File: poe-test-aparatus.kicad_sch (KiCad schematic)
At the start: 31 parts, among them J1 Power Injector, J2 PoE Header, U3 MP8007, U4 POE70P-12L

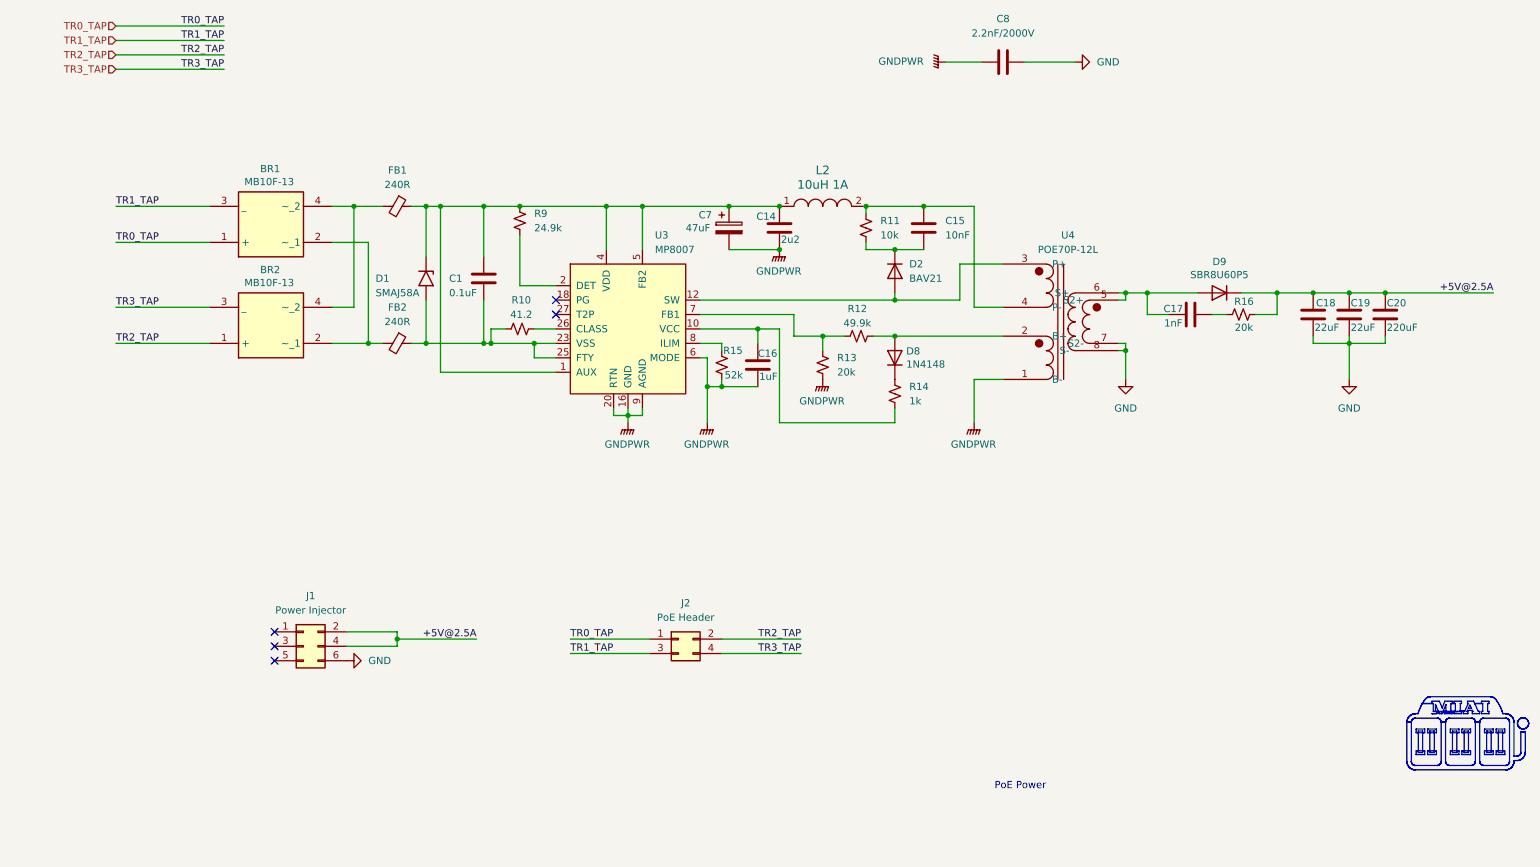
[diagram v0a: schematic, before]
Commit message: Rework with better layout and resistors fix tests
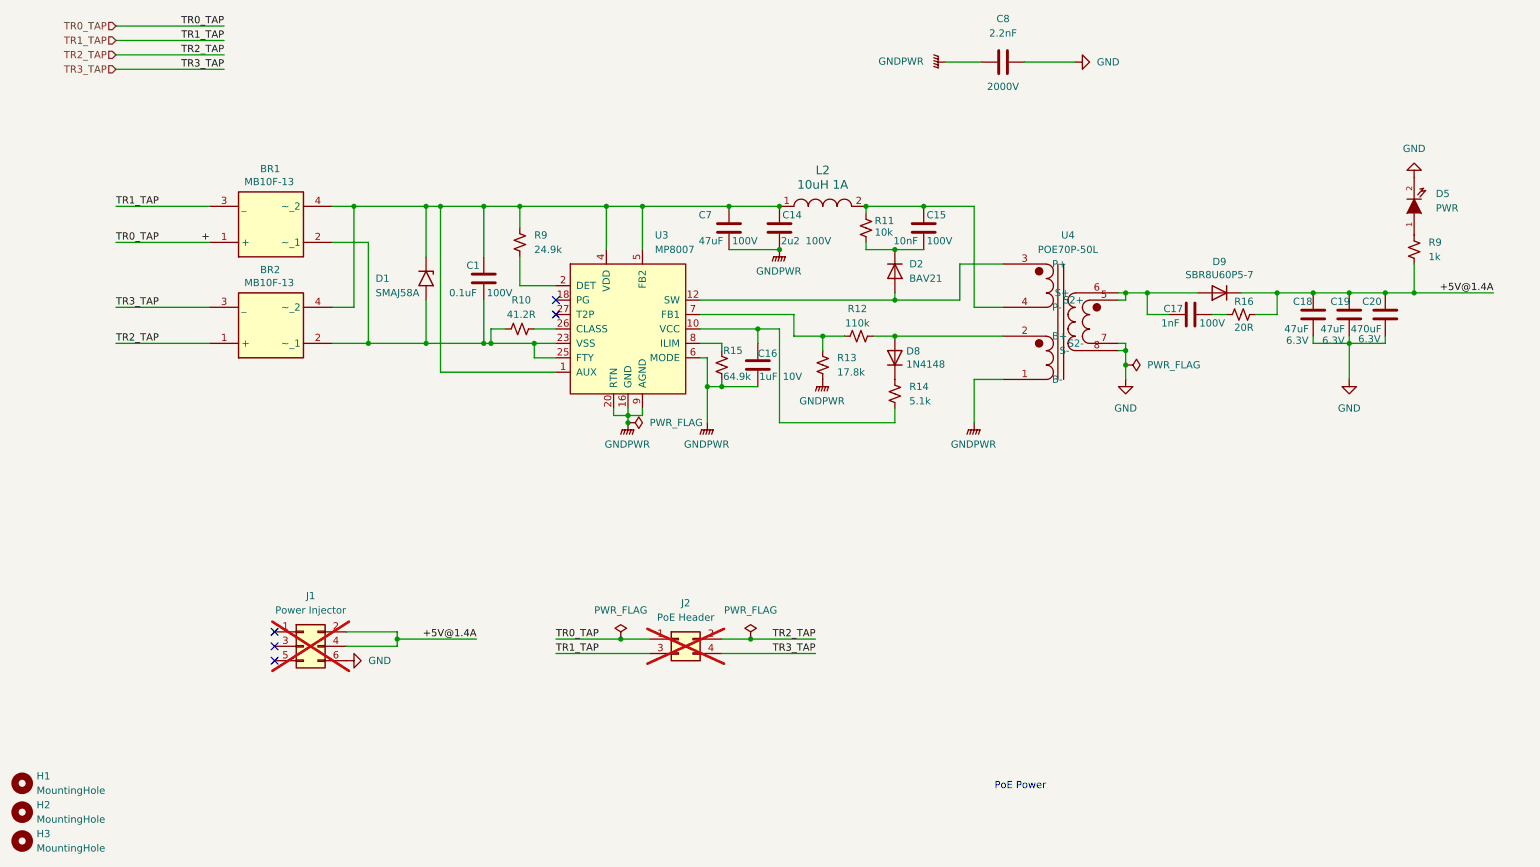
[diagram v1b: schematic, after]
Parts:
- removed FB1, FB2: 240R, PowerManagement:BLM31KN102BH1L, symbol Device:FerriteBead_Small
- added D5: PWR, LED_SMD:LED_1206_3216Metric, symbol tinkerforge:LED
- added H1, H2, H3: MountingHole, MountingHole:MountingHole_3.2mm_M3_ISO14580, symbol Mechanical:MountingHole
- added R9: 1k, Resistor_SMD:R_1206_3216Metric_Pad1.30x1.75mm_HandSolder, symbol Device:R_Small_US
- C1, C14, C15, C17: Voltage (none) -> 100V
- C16: Voltage (none) -> 10V
- C18, C19: value 22uF -> 47uF; Voltage (none) -> 6.3V
- C20: value 220uF -> 470uF; footprint Capacitor_SMD:C_1206_3216Metric_Pad1.33x1.80mm_HandSolder -> Capacitor_Tantalum_SMD:CP_EIA-7343-43_Kemet-X; Voltage (none) -> 6.3V
- C7: footprint Capacitor_SMD:CP_Elec_5x5.4 -> Capacitor_SMD:C_1210_3225Metric; symbol Device:C_Polarized -> Device:C; Voltage (none) -> 100V
- C8: value 2.2nF/2000V -> 2.2nF; footprint Capacitor_SMD:C_1206_3216Metric_Pad1.33x1.80mm_HandSolder -> Capacitor_SMD:C_1825_4564Metric; Voltage (none) -> 2000V
- D9: value SBR8U60P5 -> SBR8U60P5-7
- J1, J2: now not fitted
- L2: footprint Inductor_SMD:L_Bourns_SRU5016_5.2x5.2mm -> InductorAlt:INDPM3532X120N
- R10: value 41.2 -> 41.2R
- R12: value 49.9k -> 110k
- R13: value 20k -> 17.8k
- R14: value 1k -> 5.1k
- R15: value 52k -> 64.9k
- R16: value 20k -> 20R
- U4: value POE70P-12L -> POE70P-50L; footprint PoweredDevices:POE70P12LD -> PoweredDevices:POE70P50LD
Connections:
- net GND: now also D5.2 (K)
- net at C1.1, C14.1, C7.1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: now also BR1.4 (~_2), BR2.4 (~_2)
- net at C1.2, D1.2 (A2), R10.1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: now also BR1.2 (~_1), BR2.2 (~_1)
- net +5V@2.5A renamed +5V@1.4A
- net +5V@1.4A: now also R9.2
- new net: D5.1 (A), R9.1
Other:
- moved on the sheet: R9

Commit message: moderate updates
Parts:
- removed L2: 10uH 1A, InductorAlt:INDPM3532X120N, symbol tinkerforge:INDUCTOR
- added J3: Conn_01x02_Pin, Connector_JST:JST_SH_SM02B-SRSS-TB_1x02-1MP_P1.00mm_Horizontal, symbol Connector:Conn_01x02_Pin
- C7: value 47uF -> 10uF
- R14: value 5.1k -> 1k
- R15: value 64.9k -> 49.9k
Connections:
- net +5V@1.4A: now also J3.1 (Pin_1); no longer R9.2
- net GND: now also J3.2 (Pin_2); no longer D5.2 (K)
- net at BR1.4 (~_2), BR2.4 (~_2), C1.1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: now also C15.1, R11.1, R9.1, U4.4 (P-)
- net at U3.27 (T2P): now also D5.2 (K)
- net at D5.1 (A): now also R9.2; no longer R9.1
- net TR0_TAP renamed +
- no-connect marks 5 -> 4
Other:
- moved on the sheet: C1, R9

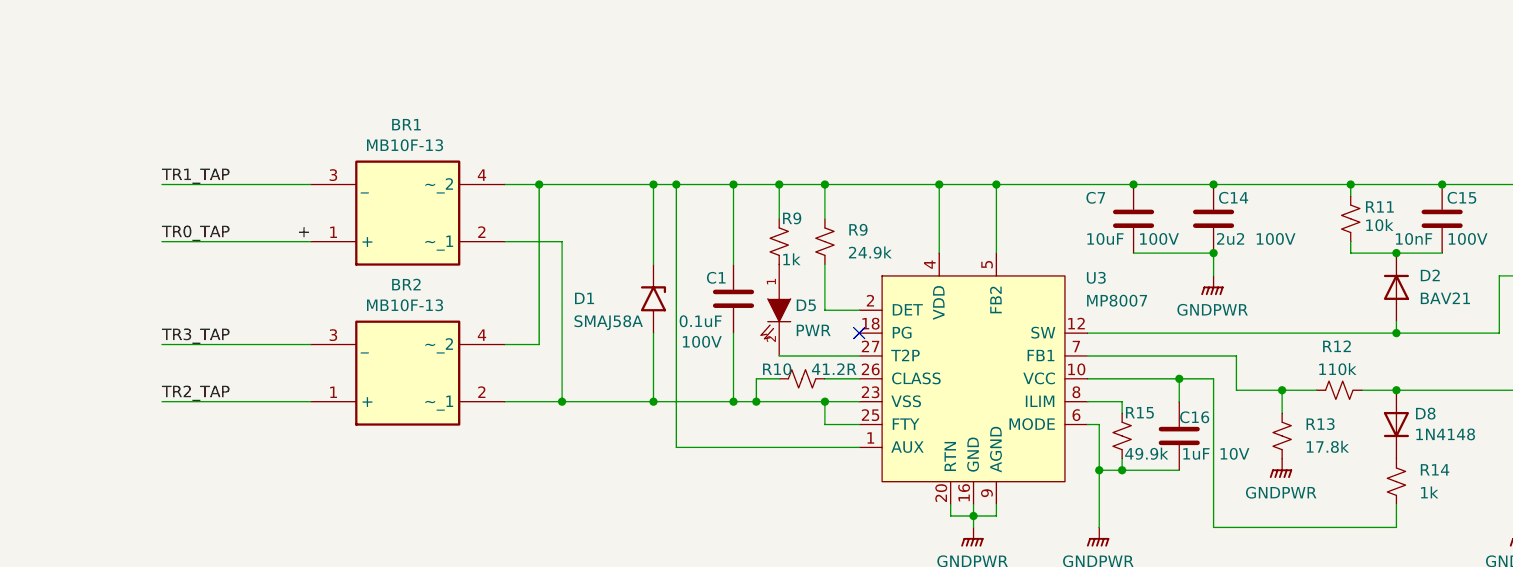
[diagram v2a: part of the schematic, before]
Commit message: Fixed flipped rectifier diode input
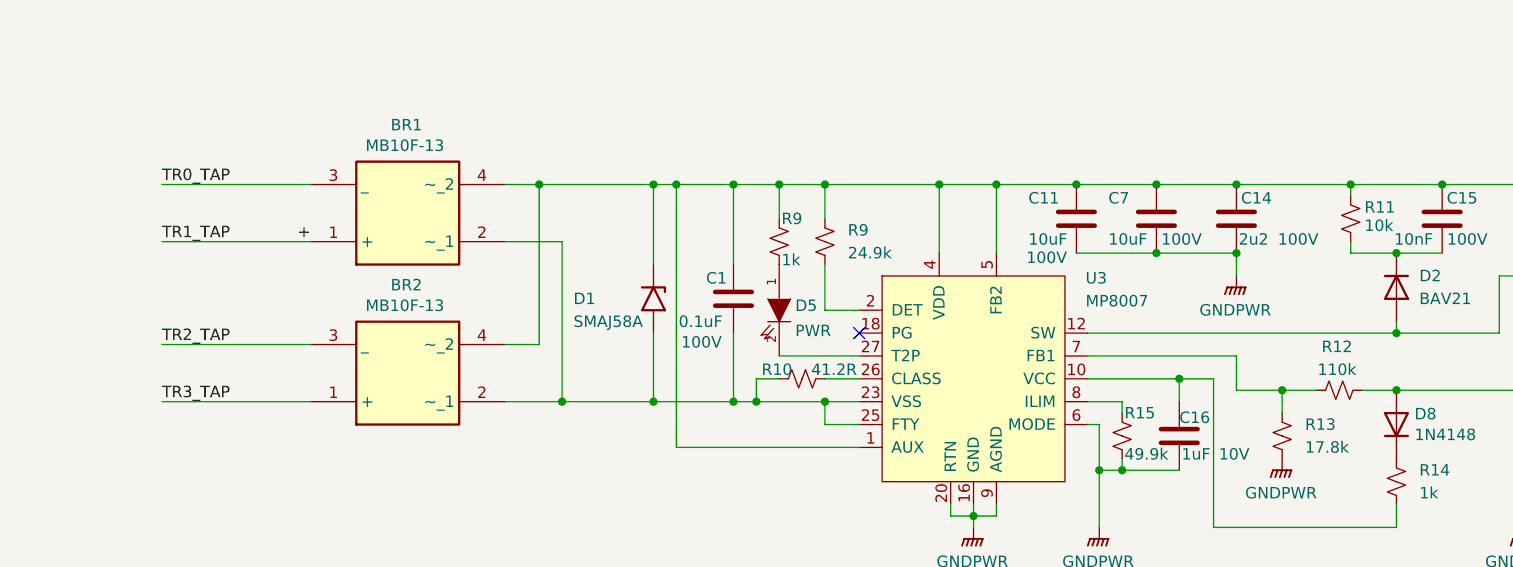
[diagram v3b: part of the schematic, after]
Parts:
- added C11: 10uF, Capacitor_SMD:C_1210_3225Metric, symbol Device:C
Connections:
- net +: now also J2.3 (Pin_3); no longer J2.1 (Pin_1)
- net GNDPWR: now also C11.2
- net TR2_TAP: now also BR2.3 (_); no longer BR2.1 (+)
- net TR3_TAP: now also BR2.1 (+); no longer BR2.3 (_)
- net at BR1.4 (~_2), BR2.4 (~_2), C1.1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: now also C11.1
- net TR1_TAP renamed TR0_TAP
- net TR0_TAP: now also J2.1 (Pin_1); no longer J2.3 (Pin_3)
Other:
- moved on the sheet: C14, C7
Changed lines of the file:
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@@
 	)
 	(junction
-		(at 212.09 106.68)
+		(at 144.78 81.28)
 		(diameter 0)
 		(color 0 0 0 0)
 	)
 	(junction
-		(at 212.09 96.52)
+		(at 212.09 106.68)
 		(diameter 0)
 		(color 0 0 0 0)
 	)
 	(junction
-		(at 158.75 104.14)
+		(at 212.09 96.52)
 		(diameter 0)
 		(color 0 0 0 0)
 	)
 	(junction
-		(at 171.45 97.79)
+		(at 158.75 104.14)
 		(diameter 0)
 		(color 0 0 0 0)
 	)
 	(junction
-		(at 151.13 81.28)
+		(at 171.45 97.79)
 		(diameter 0)
 		(color 0 0 0 0)
@@
 	)
 	(junction
+		(at 153.67 81.28)
+		(diameter 0)
+		(color 0 0 0 0)
+	)
+	(junction
+		(at 135.89 81.28)
+		(diameter 0)
+		(color 0 0 0 0)
+	)
+	(junction
 		(at 107.95 105.41)
 		(diameter 0)
@@
 	)
 	(junction
-		(at 151.13 88.9)
+		(at 153.67 88.9)
 		(diameter 0)
 		(color 0 0 0 0)
@@
 	)
 	(junction
-		(at 142.24 81.28)
+		(at 144.78 88.9)
 		(diameter 0)
 		(color 0 0 0 0)
@@
 	(wire
 		(pts
-			(xy 151.13 81.28) (xy 166.37 81.28)
-		)
-		(stroke
-			(width 0)
-			(type default)
-		)
-	)
-	(wire
-		(pts
 			(xy 100.33 105.41) (xy 107.95 105.41)
 		)
@@
 	(wire
 		(pts
+			(xy 144.78 81.28) (xy 153.67 81.28)
+		)
+		(stroke
+			(width 0)
+			(type default)
+		)
+	)
+	(wire
+		(pts
 			(xy 72.39 81.28) (xy 76.2 81.28)
 		)
@@
 	(wire
 		(pts
-			(xy 142.24 81.28) (xy 151.13 81.28)
-		)
-		(stroke
-			(width 0)
-			(type default)
-		)
-	)
-	(wire
-		(pts
 			(xy 107.95 95.25) (xy 111.76 95.25)
 		)
@@
 	(wire
 		(pts
-			(xy 151.13 88.9) (xy 151.13 91.44)
+			(xy 153.67 88.9) (xy 153.67 91.44)
 		)
 		(stroke
@@
 	(wire
 		(pts
+			(xy 135.89 88.9) (xy 144.78 88.9)
+		)
+		(stroke
+			(width 0)
+			(type default)
+		)
+	)
+	(wire
+		(pts
 			(xy 107.95 102.87) (xy 111.76 102.87)
 		)
@@
 	(wire
 		(pts
+			(xy 153.67 81.28) (xy 166.37 81.28)
+		)
+		(stroke
+			(width 0)
+			(type default)
+		)
+	)
+	(wire
+		(pts
 			(xy 34.29 99.06) (xy 50.8 99.06)
 		)
@@
 	(wire
 		(pts
-			(xy 142.24 88.9) (xy 151.13 88.9)
+			(xy 135.89 81.28) (xy 144.78 81.28)
+		)
+		(stroke
+			(width 0)
+			(type default)
+		)
+	)
+	(wire
+		(pts
+			(xy 144.78 88.9) (xy 153.67 88.9)
 		)
 		(stroke
@@
 	(wire
 		(pts
-			(xy 127 81.28) (xy 142.24 81.28)
+			(xy 127 81.28) (xy 135.89 81.28)
 		)
 		(stroke
@@
 		)
 	)
-	(label "TR1_TAP"
-		(at 116.84 160.02 0)
+	(label "TR3_TAP"
+		(at 34.29 105.41 0)
 		(fields_autoplaced yes)
 		(effects
@@
 	)
 	(label "TR1_TAP"
-		(at 34.29 81.28 0)
+		(at 116.84 160.02 0)
 		(fields_autoplaced yes)
 		(effects
@@
 		)
 	)
-	(label "+5V@1.4A"
-		(at 95.25 157.48 180)
+	(label "TR0_TAP"
+		(at 34.29 81.28 0)
 		(fields_autoplaced yes)
 		(effects
@@
 				(size 1.27 1.27)
 			)
-			(justify right bottom)
+			(justify left bottom)
 		)
 	)
-	(label "TR3_TAP"
-		(at 152.4 160.02 180)
+	(label "+5V@1.4A"
+		(at 95.25 157.48 180)
 		(fields_autoplaced yes)
 		(effects
@@
 		)
 	)
-	(label "TR0_TAP"
-		(at 116.84 157.48 0)
+	(label "TR1_TAP"
+		(at 34.29 87.63 0)
 		(fields_autoplaced yes)
 		(effects
@@
 		)
 	)
-	(label "+5V@1.4A"
-		(at 276.86 96.52 180)
+	(label "TR2_TAP"
+		(at 34.29 99.06 0)
 		(fields_autoplaced yes)
 		(effects
@@
 				(size 1.27 1.27)
 			)
-			(justify right bottom)
+			(justify left bottom)
 		)
 	)
-	(label "TR2_TAP"
-		(at 34.29 105.41 0)
+	(label "TR3_TAP"
+		(at 152.4 160.02 180)
 		(fields_autoplaced yes)
 		(effects
@@
 				(size 1.27 1.27)
 			)
-			(justify left bottom)
+			(justify right bottom)
 		)
 	)
-	(label "TR3_TAP"
-		(at 34.29 99.06 0)
+	(label "TR0_TAP"
+		(at 116.84 157.48 0)
 		(fields_autoplaced yes)
 		(effects
@@
 		)
 	)
-	(label "TR0_TAP"
-		(at 34.29 87.63 0)
+	(label "+5V@1.4A"
+		(at 276.86 96.52 180)
 		(fields_autoplaced yes)
 		(effects
@@
 				(size 1.27 1.27)
 			)
-			(justify left bottom)
+			(justify right bottom)
 		)
 	)
@@
 	(symbol
 		(lib_id "Device:C")
-		(at 142.24 85.09 0)
+		(at 144.78 85.09 0)
 		(unit 1)
 		(exclude_from_sim no)
@@
 		(dnp no)
 		(property "Reference" "C7"
-			(at 136.906 82.804 0)
+			(at 139.446 82.804 0)
 			(effects
 				(font
@@
 		)
 		(property "Value" "10uF"
-			(at 136.906 87.376 0)
+			(at 139.446 87.376 0)
 			(effects
 				(font
@@
 		)
 		(property "Footprint" "Capacitor_SMD:C_1210_3225Metric"
-			(at 143.2052 88.9 0)
+			(at 145.7452 88.9 0)
 			(effects
 				(font
@@
 		)
 		(property "Datasheet" "~"
-			(at 142.24 85.09 0)
+			(at 144.78 85.09 0)
 			(effects
 				(font
@@
 		)
 		(property "Description" "Unpolarized capacitor"
-			(at 142.24 85.09 0)
+			(at 144.78 85.09 0)
 			(effects
 				(font
@@
 		)
 		(property "Voltage" "100V"
-			(at 145.034 87.376 0)
+			(at 147.574 87.376 0)
 			(effects
 				(font
@@
 	(symbol
 		(lib_id "Device:C")
-		(at 151.13 85.09 0)
+		(at 153.67 85.09 0)
 		(unit 1)
 		(exclude_from_sim no)
@@
 		(dnp no)
 		(property "Reference" "C14"
-			(at 151.638 82.804 0)
+			(at 154.178 82.804 0)
 			(effects
 				(font
@@
 		)
 		(property "Value" "2u2"
-			(at 151.384 87.376 0)
+			(at 153.924 87.376 0)
 			(effects
 				(font
@@
 		)
 		(property "Footprint" "Capacitor_SMD:C_1206_3216Metric_Pad1.33x1.80mm_HandSolder"
-			(at 152.0952 88.9 0)
+			(at 154.6352 88.9 0)
 			(effects
 				(font
@@
 		)
 		(property "Datasheet" "~"
-			(at 151.13 85.09 0)
+			(at 153.67 85.09 0)
 			(effects
 				(font
@@
 		)
 		(property "Description" "Unpolarized capacitor"
-			(at 151.13 85.09 0)
+			(at 153.67 85.09 0)
 			(effects
 				(font
@@
 		)
 		(property "Voltage" "100V"
-			(at 157.988 87.376 0)
+			(at 160.528 87.376 0)
 			(effects
 				(font
@@
 	(symbol
 		(lib_id "power:GNDPWR")
-		(at 151.13 91.44 0)
+		(at 153.67 91.44 0)
 		(unit 1)
 		(exclude_from_sim no)
@@
 		(fields_autoplaced yes)
 		(property "Reference" "#PWR012"
-			(at 151.13 96.52 0)
+			(at 153.67 96.52 0)
 			(effects
 				(font
@@
 		)
 		(property "Value" "GNDPWR"
-			(at 151.003 95.25 0)
+			(at 153.543 95.25 0)
 			(effects
 				(font
@@
 		)
 		(property "Footprint" ""
-			(at 151.13 92.71 0)
+			(at 153.67 92.71 0)
 			(effects
 				(font
@@
 		)
 		(property "Datasheet" ""
-			(at 151.13 92.71 0)
+			(at 153.67 92.71 0)
 			(effects
 				(font
@@
 		)
 		(property "Description" "Power symbol creates a global label with name \"GNDPWR\" , global ground"
-			(at 151.13 91.44 0)
+			(at 153.67 91.44 0)
 			(effects
 				(font
@@
 					(unit 1)
 				)
+			)
+		)
+	)
+	(symbol
+		(lib_id "Device:C")
+		(at 135.89 85.09 0)
+		(unit 1)
+		(exclude_from_sim no)
+		(in_bom yes)
+		(on_board yes)
+		(dnp no)
+		(property "Reference" "C11"
+			(at 130.556 82.804 0)
+			(effects
+				(font
+					(size 1.27 1.27)
+				)
+				(justify left)
+			)
+		)
+		(property "Value" "10uF"
+			(at 130.556 87.376 0)
+			(effects
+				(font
+					(size 1.27 1.27)
+				)
+				(justify left)
+			)
+		)
+		(property "Footprint" "Capacitor_SMD:C_1210_3225Metric"
+			(at 136.8552 88.9 0)
+			(effects
+				(font
+					(size 1.27 1.27)
+				)
+				(hide yes)
+			)
+		)
+		(property "Datasheet" "~"
+			(at 135.89 85.09 0)
+			(effects
+				(font
+					(size 1.27 1.27)
+				)
+				(hide yes)
+			)
+		)
+		(property "Description" "Unpolarized capacitor"
+			(at 135.89 85.09 0)
+			(effects
+				(font
+					(size 1.27 1.27)
+				)
+				(hide yes)
+			)
+		)
+		(property "Voltage" "100V"
+			(at 132.588 89.408 0)
+			(effects
+				(font
+					(size 1.27 1.27)
+				)
+			)
+		)
+		(pin "1"
+		)
+		(pin "2"
+		)
+		(instances
+			(project "poe-test-aparatus"
+				(path "/f685a4d7-fe27-4c6a-bf30-4186c3981db2"
+					(reference "C11")
+					(unit 1)
+				)

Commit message: adjust resistor value
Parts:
- R14: value 1k -> 5.1k
- R15: value 49.9k -> 64.9k
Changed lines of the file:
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@@
 			)
 		)
-		(property "Value" "49.9k"
+		(property "Value" "64.9k"
 			(at 141.224 111.252 0)
 			(effects
@@
 			)
 		)
-		(property "Value" "1k"
+		(property "Value" "5.1k"
 			(at 173.99 115.5699 0)
 			(effects
